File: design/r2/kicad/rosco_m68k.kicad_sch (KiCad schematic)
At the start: 0 parts

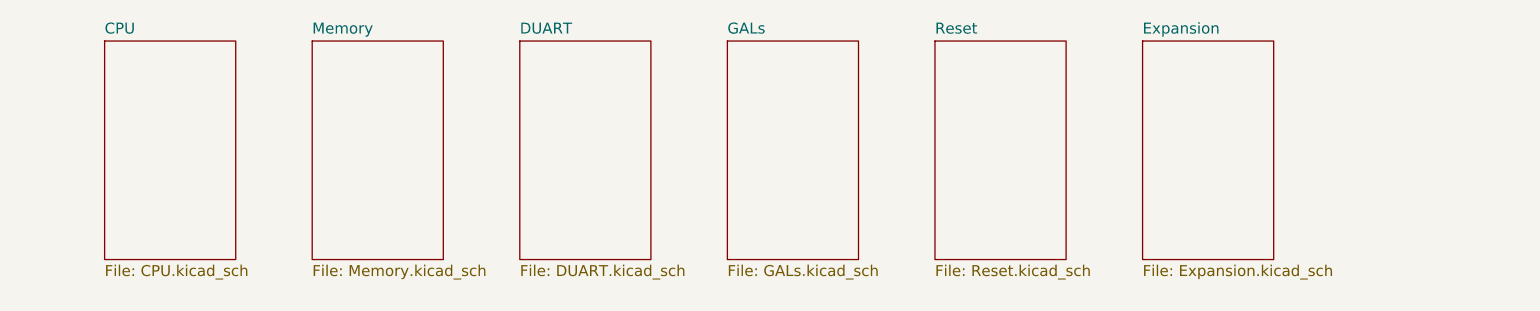
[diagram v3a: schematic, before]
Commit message: Feature/smd birdseed (#427)
* GAL changes to better support coprocessor

* Update designs for copro GAL change

* Revert accidental DUARTSEL changes

* Re-add mistakenly-removed polarity symbols

* Tentative r2 SMD design

* Resize tiny resistors

* More address lines into GALs

* Reroute for FTDI

* prod

* Correct FT2232HL part number

* Mask expansion and silk tidy after first spin
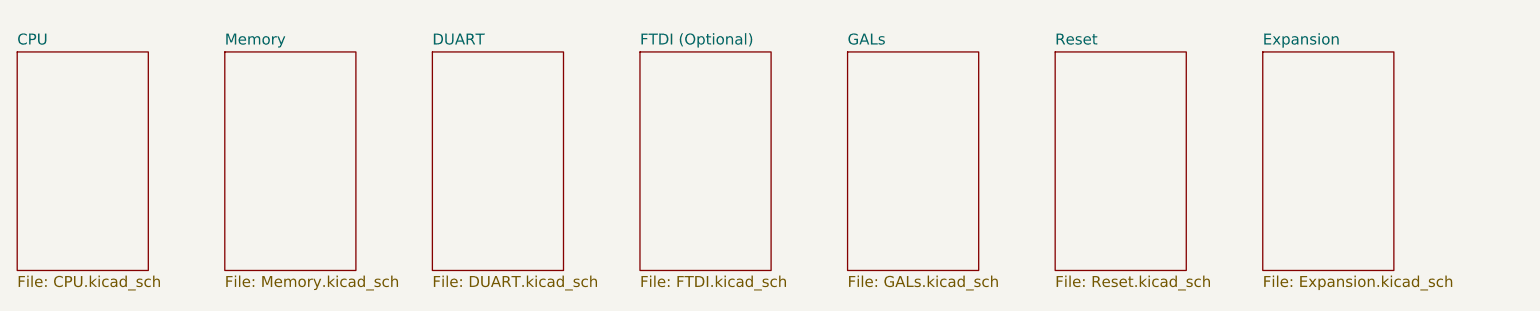
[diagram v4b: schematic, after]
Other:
- added sheet FTDI (Optional) (FTDI.kicad_sch)
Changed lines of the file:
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@@
   (title_block
     (title "ROSCO_M68K GENERAL PURPOSE MC68010 COMPUTER")
-    (date "2024-03-09")
+    (date "2024-04-15")
     (rev "2.2")
     (company "The Really Old-School Company Limited")
@@
     (comment 4 "Copyright 2019-2024 Ross Bamford and Contributors")
   )
-  (sheet (at 81.28 81.28) (size 15.24 25.4) (fields_autoplaced)
+  (sheet (at 71.12 82.55) (size 15.24 25.4) (fields_autoplaced)
     (stroke (width 0) (type solid))
     (fill (color 0 0 0 0.0000))
-    (property "Sheetname" "CPU" (at 81.28 80.5684 0)
+    (property "Sheetname" "CPU" (at 71.12 81.8384 0)
       (effects (font (size 1.27 1.27)) (justify left bottom))
     )
-    (property "Sheetfile" "CPU.kicad_sch" (at 81.28 107.2646 0)
+    (property "Sheetfile" "CPU.kicad_sch" (at 71.12 108.5346 0)
       (effects (font (size 1.27 1.27)) (justify left top))
     )
@@
     )
   )
-  (sheet (at 201.93 81.28) (size 15.24 25.4) (fields_autoplaced)
+  (sheet (at 215.9 82.55) (size 15.24 25.4) (fields_autoplaced)
     (stroke (width 0) (type solid))
     (fill (color 0 0 0 0.0000))
-    (property "Sheetname" "Expansion" (at 201.93 80.5684 0)
+    (property "Sheetname" "Expansion" (at 215.9 81.8384 0)
       (effects (font (size 1.27 1.27)) (justify left bottom))
     )
-    (property "Sheetfile" "Expansion.kicad_sch" (at 201.93 107.2646 0)
+    (property "Sheetfile" "Expansion.kicad_sch" (at 215.9 108.5346 0)
       (effects (font (size 1.27 1.27)) (justify left top))
     )
@@
     )
   )
-  (sheet (at 129.54 81.28) (size 15.24 25.4) (fields_autoplaced)
+  (sheet (at 119.38 82.55) (size 15.24 25.4) (fields_autoplaced)
     (stroke (width 0) (type solid))
     (fill (color 0 0 0 0.0000))
-    (property "Sheetname" "DUART" (at 129.54 80.5684 0)
+    (property "Sheetname" "DUART" (at 119.38 81.8384 0)
       (effects (font (size 1.27 1.27)) (justify left bottom))
     )
-    (property "Sheetfile" "DUART.kicad_sch" (at 129.54 107.2646 0)
+    (property "Sheetfile" "DUART.kicad_sch" (at 119.38 108.5346 0)
       (effects (font (size 1.27 1.27)) (justify left top))
     )
@@
     )
   )
-  (sheet (at 177.8 81.28) (size 15.24 25.4) (fields_autoplaced)
+  (sheet (at 191.77 82.55) (size 15.24 25.4) (fields_autoplaced)
     (stroke (width 0) (type solid))
     (fill (color 0 0 0 0.0000))
-    (property "Sheetname" "Reset" (at 177.8 80.5684 0)
+    (property "Sheetname" "Reset" (at 191.77 81.8384 0)
       (effects (font (size 1.27 1.27)) (justify left bottom))
     )
-    (property "Sheetfile" "Reset.kicad_sch" (at 177.8 107.2646 0)
+    (property "Sheetfile" "Reset.kicad_sch" (at 191.77 108.5346 0)
       (effects (font (size 1.27 1.27)) (justify left top))
     )
@@
     )
   )
-  (sheet (at 105.41 81.28) (size 15.24 25.4) (fields_autoplaced)
+  (sheet (at 95.25 82.55) (size 15.24 25.4) (fields_autoplaced)
     (stroke (width 0) (type solid))
     (fill (color 0 0 0 0.0000))
-    (property "Sheetname" "Memory" (at 105.41 80.5684 0)
+    (property "Sheetname" "Memory" (at 95.25 81.8384 0)
       (effects (font (size 1.27 1.27)) (justify left bottom))
     )
-    (property "Sheetfile" "Memory.kicad_sch" (at 105.41 107.2646 0)
+    (property "Sheetfile" "Memory.kicad_sch" (at 95.25 108.5346 0)
       (effects (font (size 1.27 1.27)) (justify left top))
     )
@@
     )
   )
-  (sheet (at 153.67 81.28) (size 15.24 25.4) (fields_autoplaced)
+  (sheet (at 167.64 82.55) (size 15.24 25.4) (fields_autoplaced)
     (stroke (width 0) (type solid))
     (fill (color 0 0 0 0.0000))
-    (property "Sheetname" "GALs" (at 153.67 80.5684 0)
+    (property "Sheetname" "GALs" (at 167.64 81.8384 0)
       (effects (font (size 1.27 1.27)) (justify left bottom))
     )
-    (property "Sheetfile" "GALs.kicad_sch" (at 153.67 107.2646 0)
+    (property "Sheetfile" "GALs.kicad_sch" (at 167.64 108.5346 0)
       (effects (font (size 1.27 1.27)) (justify left top))
     )
@@
       )
     )
+  )
+  (sheet (at 143.51 82.55) (size 15.24 25.4) (fields_autoplaced)
+    (stroke (width 0.1524) (type solid))
+    (fill (color 0 0 0 0.0000))
+    (property "Sheetname" "FTDI (Optional)" (at 143.51 81.8384 0)
+      (effects (font (size 1.27 1.27)) (justify left bottom))
+    )
+    (property "Sheetfile" "FTDI.kicad_sch" (at 143.51 108.5346 0)
+      (effects (font (size 1.27 1.27)) (justify left top))
+    )
+    (instances
+      (project "rosco_m68k"
+        (path "/9031bb33-c6aa-4758-bf5c-3274ed3ebab7" (page "8"))
+      )
+    )
